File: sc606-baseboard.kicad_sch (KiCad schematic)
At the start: 6 parts

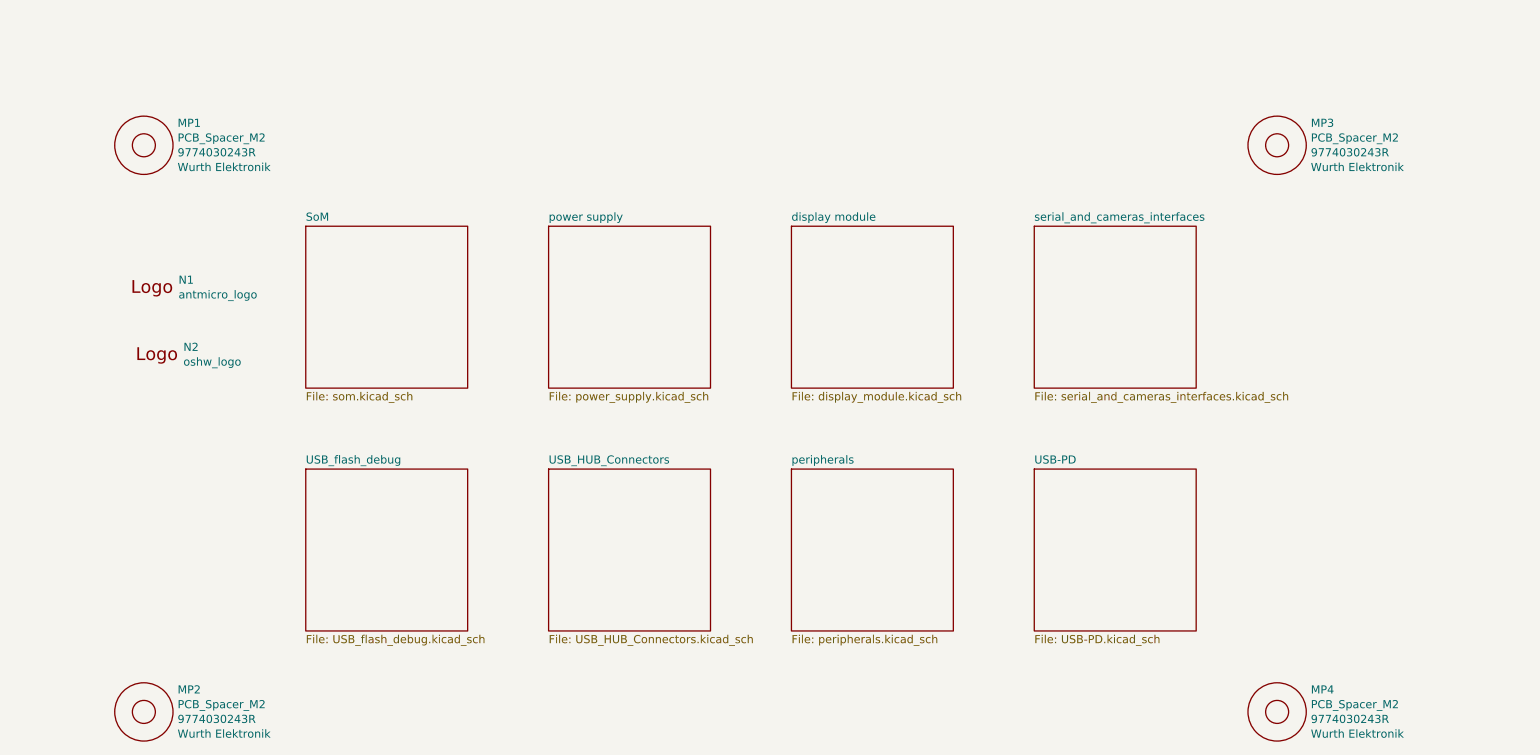
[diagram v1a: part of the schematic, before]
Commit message: Introduce component standardization
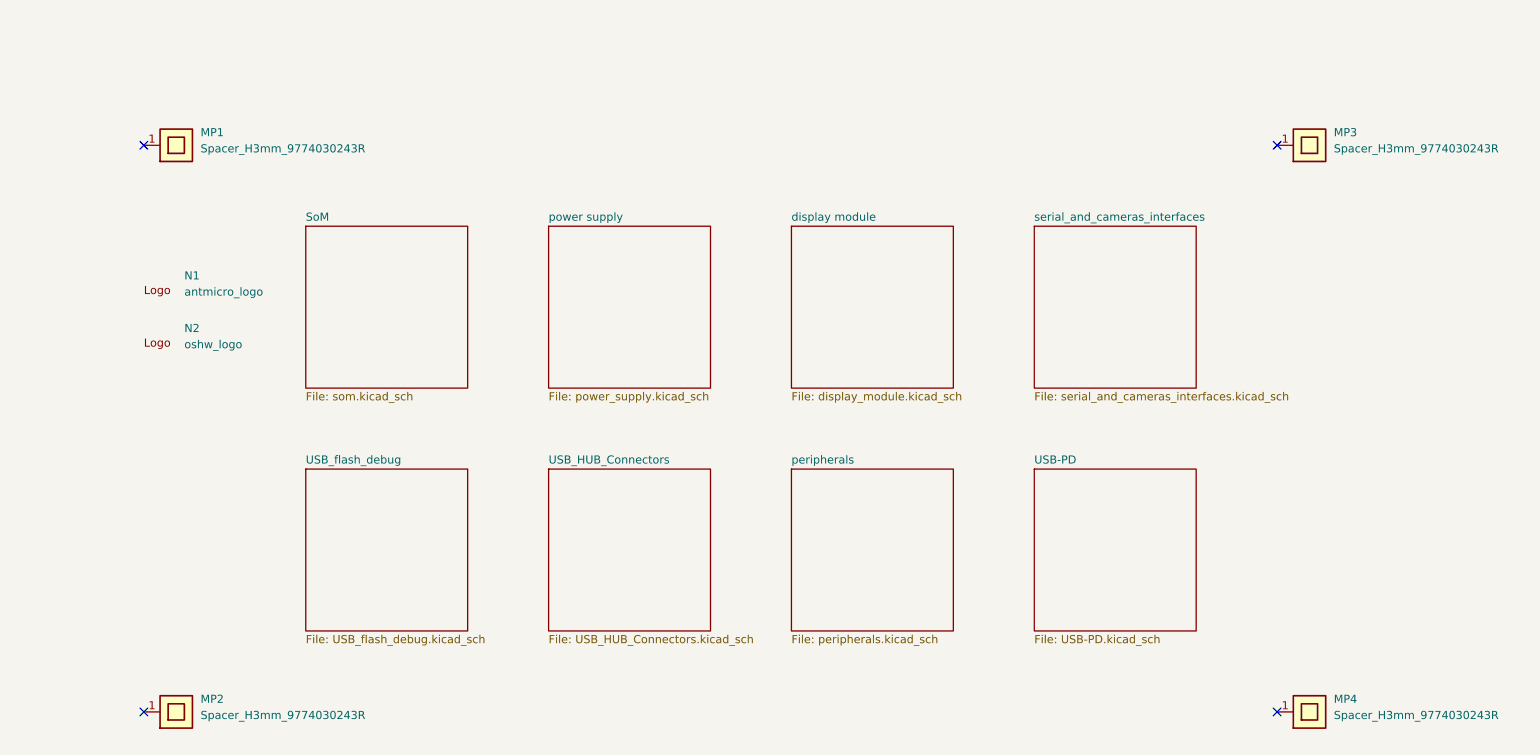
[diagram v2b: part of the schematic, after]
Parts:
- MP1, MP2, MP3, MP4: value PCB_Spacer_M2 -> Spacer_H3mm_9774030243R; footprint sc606-baseboard-footprints:9774030243R -> sc606-baseboard-footprints:Spacer_SMD_M2_H3mm_Wurth_9774030243R; symbol sc606-baseboard:PCB_Spacer_M2 -> sc606-baseboard:Spacer_H3mm_9774030243R; Author (none) -> Antmicro; License (none) -> Apache-2.0; Manufacturer Wurth Elektronik -> Würth Elektronik
- N1, N2: Author (none) -> Antmicro; License (none) -> Apache-2.0
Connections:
- no-connect marks 0 -> 4
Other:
- moved on the sheet: N1, N2

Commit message: [#61796] Run globlib
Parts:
- MP1, MP2, MP3, MP4: footprint sc606-baseboard-footprints:Spacer_SMD_M2_H3mm_Wurth_9774030243R -> antmicro-footprints:Spacer_Drill3mm_H3mm_9774030243R; symbol sc606-baseboard:Spacer_H3mm_9774030243R -> antmicroMechanicalParts:Spacer_Drill3mm_H3mm_9774030243R
- N1: footprint sc606-baseboard-footprints:antmicro-logo_scaled_12mm -> antmicro-footprints:antmicro-logo; symbol sc606-baseboard:antmicro_logo -> antmicroMechanicalParts:antmicro_logo
- N2: footprint sc606-baseboard-footprints:oshw-logo -> antmicro-footprints:oshw-logo; symbol sc606-baseboard:oshw_logo -> antmicroMechanicalParts:oshw_logo

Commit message: [#61796] Update schematics
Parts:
- MP1, MP2, MP3, MP4: value Spacer_H3mm_9774030243R -> Spacer_Drill3mm_H3mm_9774030243R
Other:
- company: (none) -> Antmicro Ltd

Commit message: [#61796] Update PCB
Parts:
- N1: footprint antmicro-footprints:antmicro-logo -> antmicro-footprints:antmicro-logo_scaled_12mm
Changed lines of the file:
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@@
       (effects (font (size 1.27 1.27) (thickness 0.15)) (justify left bottom))
     )
-    (property "Footprint" "antmicro-footprints:antmicro-logo" (at 129.54 173.355 0)
+    (property "Footprint" "antmicro-footprints:antmicro-logo_scaled_12mm" (at 129.54 173.355 0)
       (effects (font (size 1.27 1.27) (thickness 0.15)) (justify left bottom) hide)
     )
